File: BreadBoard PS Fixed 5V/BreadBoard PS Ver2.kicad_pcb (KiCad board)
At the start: 2 copper layers, 29.8 x 52 mm, 15 parts, among them J1 Barrel_Jack_Switch_MountingPin, J2 Conn_02x02_Odd_Even, J3 Conn_02x02_Odd_Even, J4 Conn_02x02_Odd_Even, J5 Conn_02x02_Odd_Even, SW1 SW_DPDT_x2, U1 LM7805_TO220

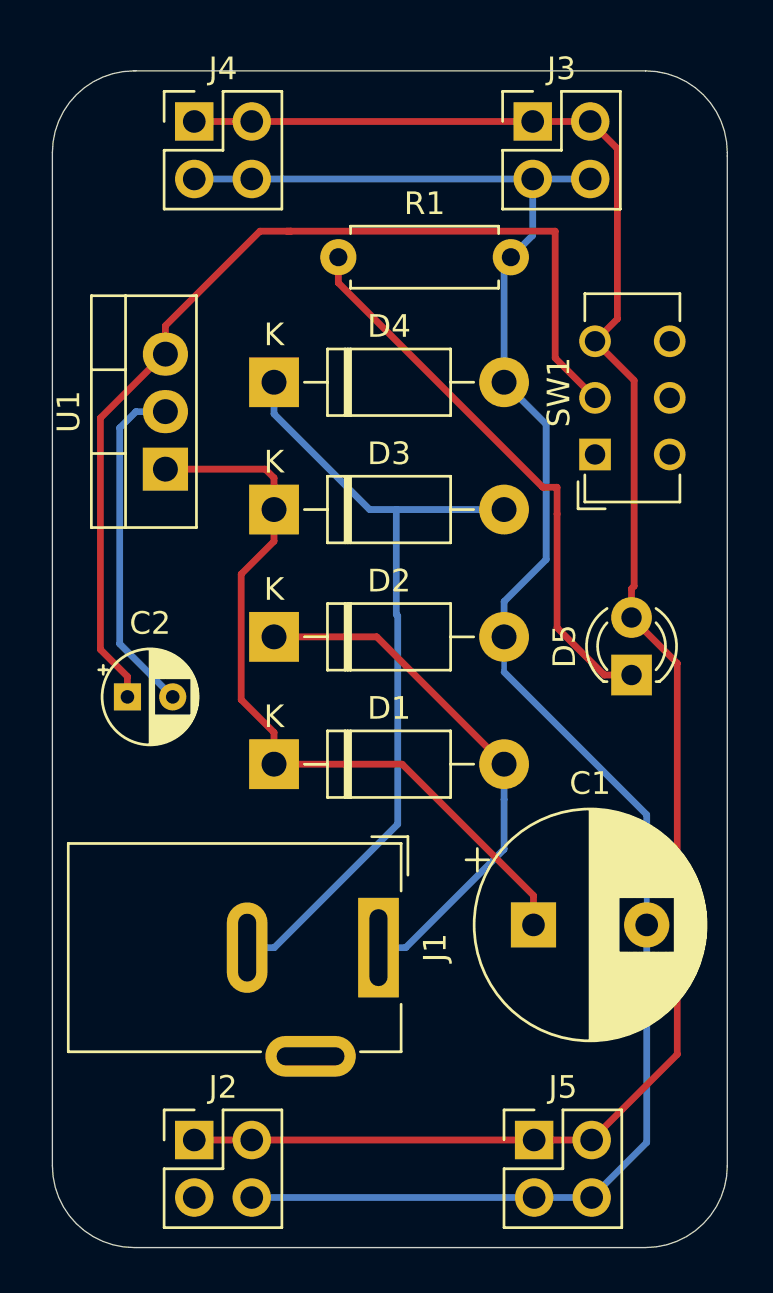
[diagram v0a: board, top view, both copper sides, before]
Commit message: Run Design Rules Check
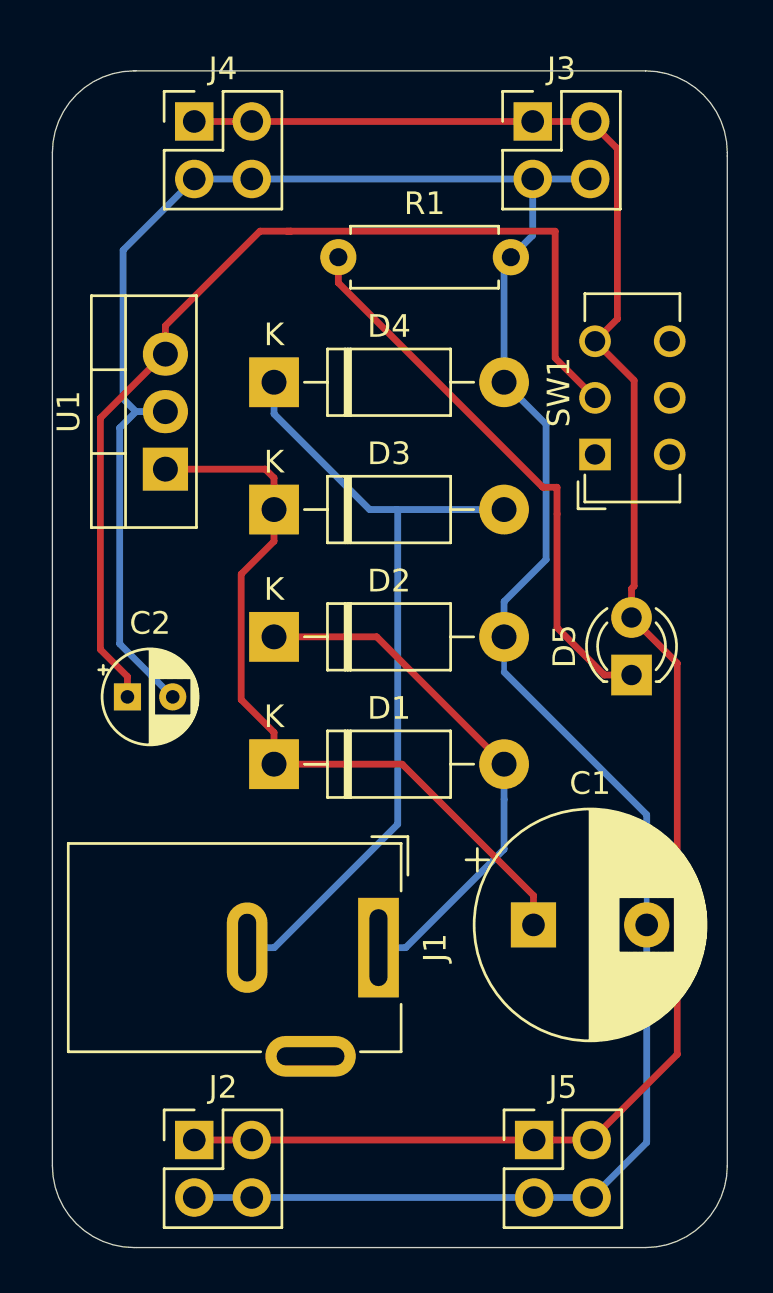
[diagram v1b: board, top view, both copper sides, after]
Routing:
- net /Gnd: track 98.3 -> 113.9 mm
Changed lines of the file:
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@@
     (thickness 1.6)
     (drawings 11)
-    (tracks 86)
+    (tracks 90)
     (zones 0)
     (modules 15)
@@
   )
   (setup
-    (last_trace_width 0.25)
+    (last_trace_width 0.3)
     (user_trace_width 0.3)
     (trace_clearance 0.2)
@@
   (segment (start 144.0942 97.3775) (end 144.0942 87.8413) (width 0.3) (layer B.Cu) (net 2))
   (segment (start 146.4371 99.7204) (end 144.0942 97.3775) (width 0.3) (layer B.Cu) (net 2))
+  (segment (start 146.1135 87.122) (end 144.8635 87.122) (width 0.25) (layer B.Cu) (net 2))
+  (segment (start 144.8135 87.122) (end 144.2466 86.5551) (width 0.3) (layer B.Cu) (net 2))
+  (segment (start 144.2466 79.9886) (end 147.3875 76.8477) (width 0.3) (layer B.Cu) (net 2))
+  (segment (start 144.2466 86.5551) (end 144.2466 79.9886) (width 0.3) (layer B.Cu) (net 2))
+  (segment (start 149.9275 121.8311) (end 147.3875 121.8311) (width 0.3) (layer B.Cu) (net 2))
   (segment (start 144.4371 98.8204) (end 143.2433 97.6266) (width 0.3) (layer F.Cu) (net 3))
   (segment (start 144.4371 99.7204) (end 144.4371 98.8204) (width 0.3) (layer F.Cu) (net 3))
@@
   (segment (start 155.133525 91.44715) (end 150.911 87.224625) (width 0.3) (layer B.Cu) (net 5))
   (segment (start 156.3116 91.4654) (end 156.32985 91.44715) (width 0.3) (layer B.Cu) (net 5))
-  (segment (start 156.3116 96.07955) (end 156.3116 91.4654) (width 0.3) (layer B.Cu) (net 5))
   (segment (start 156.32985 91.44715) (end 155.133525 91.44715) (width 0.3) (layer B.Cu) (net 5))
+  (segment (start 161.071 91.44715) (end 156.32985 91.44715) (width 0.3) (layer B.Cu) (net 5))
+  (segment (start 156.3751 91.4924) (end 156.32985 91.44715) (width 0.3) (layer B.Cu) (net 5))
+  (segment (start 156.3751 105.3439) (end 156.3751 91.4924) (width 0.3) (layer B.Cu) (net 5))
   (segment (start 149.7242 110.7948) (end 150.9242 110.7948) (width 0.3) (layer B.Cu) (net 5))
   (segment (start 150.9242 110.7948) (end 156.3751 105.3439) (width 0.3) (layer B.Cu) (net 5))
-  (segment (start 156.3751 105.3439) (end 156.3751 96.14305) (width 0.3) (layer B.Cu) (net 5))
-  (segment (start 161.071 91.44715) (end 156.32985 91.44715) (width 0.3) (layer B.Cu) (net 5))
-  (segment (start 156.3751 96.14305) (end 156.3116 96.07955) (width 0.3) (layer B.Cu) (net 5))
   (segment (start 165.5002 98.7552) (end 163.4109 96.6659) (width 0.3) (layer F.Cu) (net 6))
   (segment (start 166.7002 98.7552) (end 165.5002 98.7552) (width 0.3) (layer F.Cu) (net 6))
